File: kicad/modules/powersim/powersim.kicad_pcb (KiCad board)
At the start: 2 copper layers, 84.6 x 64 mm, 61 parts, among them J1 Bus_PCI_Express_x1, J4 Conn_01x02, J6 USB_C_Receptacle_USB2.0_16P, U2 RP2040, U4 W25Q128JVP, U5 BMP388, U8 BNO055, U9 MCP25625T-E/ML, X1 ABM8-272-T3, Y1 ABS07-32.768KHZ-T, Y2 X322516MLB4SI

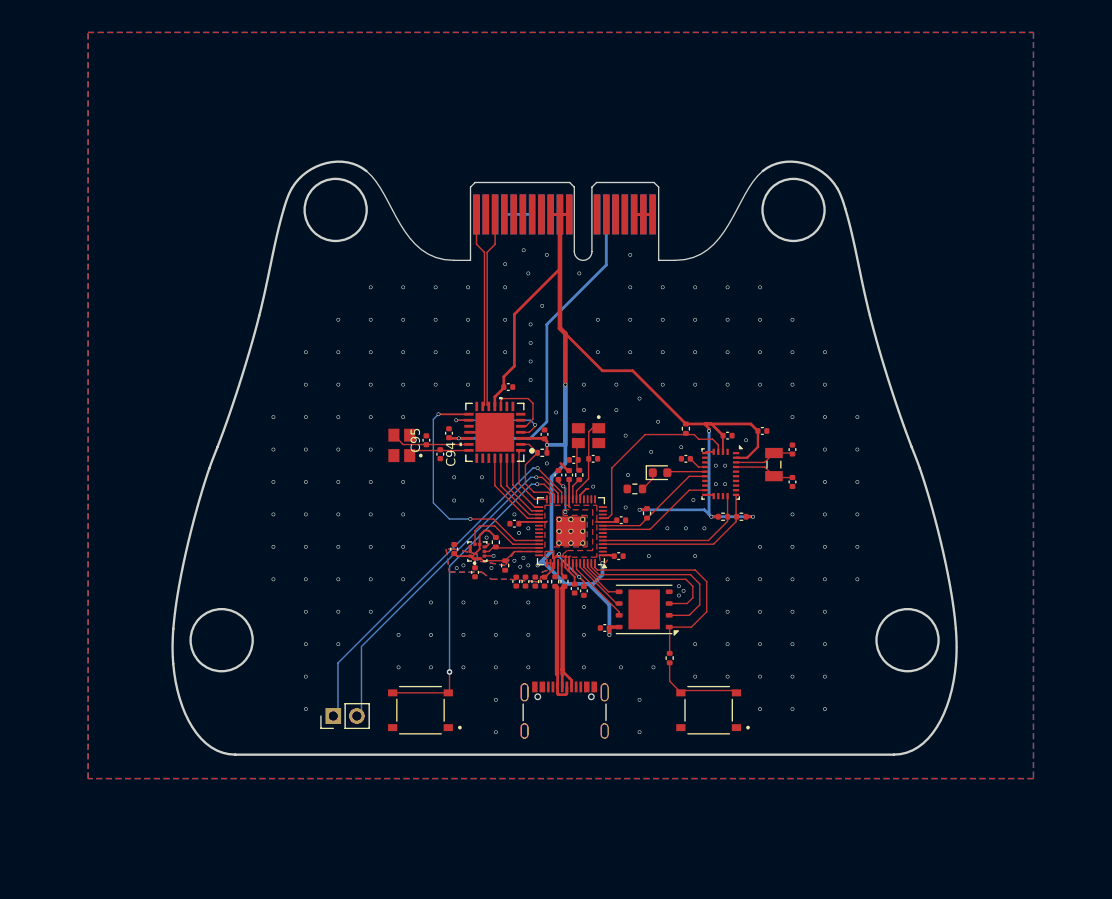
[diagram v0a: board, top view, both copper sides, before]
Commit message: powersim: add all components to schematic
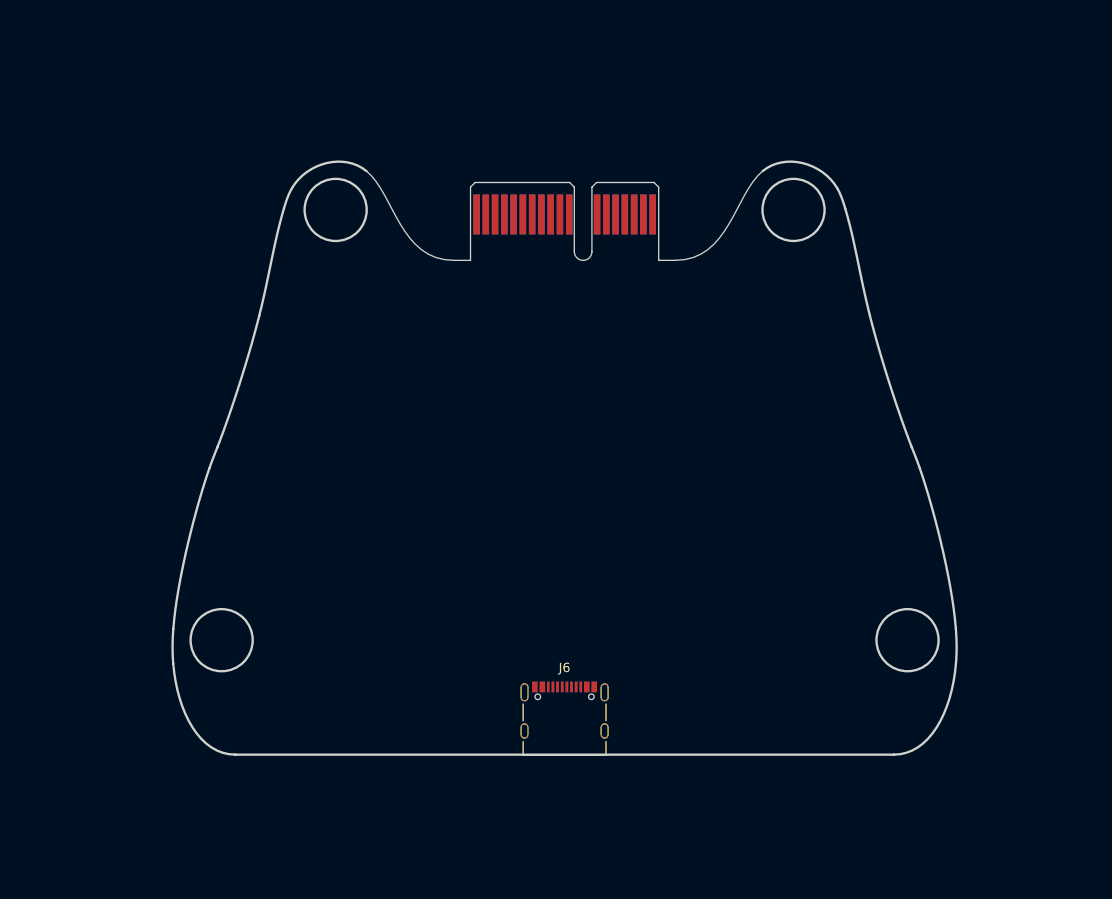
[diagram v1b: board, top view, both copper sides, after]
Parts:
- removed ? (x9): , 
- removed C10, C11: 15p, Capacitor_SMD:C_0402_1005Metric
- removed C206, C207, C209, C211, C212, C213, C214, C215, C216, C40, C50, C51, C81, C82, C90, C92, C93: 100n, Capacitor_SMD:C_0402_1005Metric
- removed C208, C210, C84: 1u, Capacitor_SMD:C_0402_1005Metric
- removed C85, C86, C94, C95: 22p, Capacitor_SMD:C_0402_1005Metric
- removed D88: LED, LED_SMD:LED_0603_1608Metric
- removed J4: Conn_01x02, Connector_PinHeader_2.54mm:PinHeader_1x02_P2.54mm_Vertical
- removed R12, R30: 1k, Resistor_SMD:R_0402_1005Metric
- removed R203, R204: 27, Resistor_SMD:R_0402_1005Metric
- removed R220, R221, R222, R223: 4.7k, Resistor_SMD:R_0402_1005Metric
- removed R83, R87, R91: 10k, Resistor_SMD:R_0402_1005Metric
- removed R89: 150, Resistor_SMD:R_0603_1608Metric
- removed S1, S2: TS-1187A-B-A-B, TS-1187A-B-A-B:SW_TS-1187A-B-A-B
- removed U2: RP2040, Package_DFN_QFN:QFN-56-1EP_7x7mm_P0.4mm_EP3.2x3.2mm
- removed U4: W25Q128JVP, Package_SON:WSON-8-1EP_6x5mm_P1.27mm_EP3.4x4.3mm
- removed U5: BMP388, BMP388:PQFN50P200X200X80-10N
- removed U8: BNO055, Package_LGA:LGA-28_5.2x3.8mm_P0.5mm
- removed U9: MCP25625T-E/ML, MCP25625T_E_ML:QFN28_6X6MC_MCH
- removed X1: ABM8-272-T3, ABM8-272-T3:ABM8-272-T3_ABR
- removed Y1: ABS07-32.768KHZ-T, ABS07-32.768KHZ-T:XTAL_ABS07-32.768KHZ-T
- removed Y2: X322516MLB4SI, X322516MLB4SI:OSC_X322516MLB4SI
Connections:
- J6 pad A4: unconnected-(J6-VBUS-PadA4)_1 -> +5V
- J6 pad A6: USB_D+ -> unconnected-(J6-D+-PadA6)
- J6 pad A7: USB_D- -> unconnected-(J6-D--PadA7)
- J6 pad A9: unconnected-(J6-VBUS-PadA4) -> +5V
- J6 pad B4: unconnected-(J6-VBUS-PadA4)_2 -> +5V
- J6 pad B6: USB_D+ -> unconnected-(J6-D+-PadB6)
- J6 pad B7: USB_D- -> unconnected-(J6-D--PadB7)
- J6 pad B9: unconnected-(J6-VBUS-PadA4)_3 -> +5V
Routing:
- net +3.3V: track 168.2 -> 0.00 mm, vias 16 -> 0
- net /SWCLK: track 40.2 -> 0.00 mm, vias 1 -> 0
- net +5V: track 37.4 -> 0.00 mm, vias 1 -> 0
- net /SWD: track 37.4 -> 0.00 mm, vias 1 -> 0
- net /RUN: track 35.6 -> 0.00 mm, vias 2 -> 0
- net CANSTBY: track 26.2 -> 0.00 mm, vias 2 -> 0
- net /QSPI_SS: track 24.0 -> 0.00 mm
- net CANP: track 21.1 -> 0.00 mm
- net CANN: track 21.1 -> 0.00 mm
- net BOOT_LOAD: track 20.3 -> 0.00 mm
- net /QSPI_SD1: track 18.9 -> 0.00 mm
- net SDA1: track 18.3 -> 0.00 mm
- net SCL1: track 17.0 -> 0.00 mm
- net /QSPI_SD2: track 16.7 -> 0.00 mm
- net +1.1V: track 15.0 -> 0.00 mm, vias 4 -> 0
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- removed copper zone on F.Cu, net +1.1V
- removed copper zone on B.Cu, net +3.3V
- removed copper zone on F.Cu, net +3.3V
- removed copper zone on B.Cu, net GND
- removed copper zone on F.Cu, net GND

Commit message: powersim: finish PCB
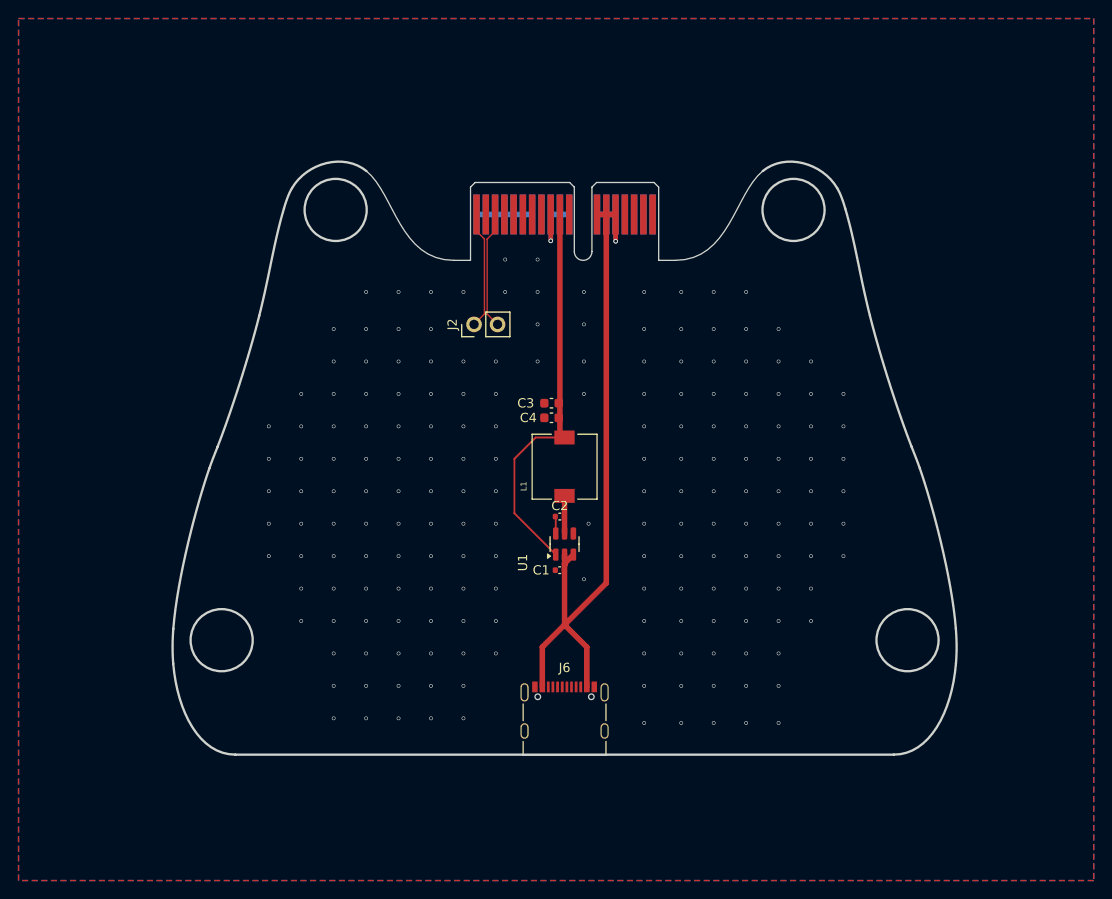
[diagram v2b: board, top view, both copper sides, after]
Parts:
- added C1: 10u, Capacitor_SMD:C_0402_1005Metric, F.Cu at (145.9, 102.5)
- added C2: 100n, Capacitor_SMD:C_0402_1005Metric, F.Cu at (145.9, 96.7)
- added C3: 22u, Capacitor_SMD:C_0603_1608Metric, F.Cu at (145.0, 84.5)
- added C4: 22u, Capacitor_SMD:C_0603_1608Metric, F.Cu at (145.0, 86.1)
- added J2: Conn_01x02_Pin, Connector_PinHeader_2.54mm:PinHeader_1x02_P2.54mm_Vertical, F.Cu at (136.6, 76.0)
- added L1: SLF7055T-6R8N2R8-3PF, SLF7055T-6R8N2R8-3PF:IND_SLF7055T-6R8N2R8-3PF, F.Cu at (146.4, 91.3)
- added U1: AP63203WU, Package_TO_SOT_SMD:TSOT-23-6, F.Cu at (146.4, 99.7)
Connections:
- J1 pad A16: +7.4V -> unconnected-(J1-PERp0-PadA16)
- J1 pad A17: +7.4V -> unconnected-(J1-PERn0-PadA17)
- J1 pad A18: +7.4V -> unconnected-(J1-GND-PadA18)
- J1 pad B16: +7.4V -> unconnected-(J1-GND-PadB16)
- J1 pad B17: +7.4V -> unconnected-(J1-~{PRSNT2}-PadB17)
- J1 pad B18: +7.4V -> unconnected-(J1-GND-PadB18)
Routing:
- net +5V: track 0.00 -> 80.3 mm, vias 0 -> 1
- net +3.3V: track 0.00 -> 50.3 mm, vias 0 -> 1
- net CANN: track 0.00 -> 12.7 mm
- net CANP: track 0.00 -> 12.7 mm
- net GND: track 0.00 -> 6.00 mm, vias 0 -> 187
- net Net-(U1-SW): track 0.00 -> 4.06 mm
- net Net-(U1-BST): track 0.00 -> 1.85 mm
- added copper zone on B.Cu, net GND
- added copper zone on F.Cu, net GND

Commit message: powersim: finish board
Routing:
- net +3.3V: track 50.3 -> 52.3 mm
- net GND: vias 187 -> 194
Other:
- board text added: "powersim 0.1.0"
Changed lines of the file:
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@@
 			(at 2.5 0 0)
 			(layer "F.SilkS")
+			(hide yes)
 			(effects
 				(font
@@
 			(at 0 1.43 0)
 			(layer "F.Fab")
+			(hide yes)
 			(effects
 				(font
@@
 			(at 0 0 0)
 			(layer "F.Fab")
+			(hide yes)
 			(effects
 				(font
@@
 			(at 2.775 0 0)
 			(layer "F.SilkS")
+			(hide yes)
 			(effects
 				(font
@@
 			(at 0 1.43 0)
 			(layer "F.Fab")
+			(hide yes)
 			(effects
 				(font
@@
 			(at 0 0 0)
 			(layer "F.Fab")
+			(hide yes)
 			(effects
 				(font
@@
 			(at 0 -4.58 0)
 			(layer "F.SilkS")
+			(hide yes)
 			(effects
 				(font
@@
 			(at 0 6.24 0)
 			(layer "F.Fab")
+			(hide yes)
 			(effects
 				(font
@@
 		(attr smd)
 		(fp_line
-			(start -4.47 -0.67)
-			(end -4.47 1.13)
-			(stroke
-				(width 0.12)
-				(type solid)
-			)
-			(layer "F.SilkS")
-		)
-		(fp_line
-			(start -4.47 4.84)
-			(end -4.47 3.38)
-			(stroke
-				(width 0.12)
-				(type solid)
-			)
-			(layer "F.SilkS")
-		)
-		(fp_line
-			(start 4.47 -0.67)
-			(end 4.47 1.13)
-			(stroke
-				(width 0.12)
-				(type solid)
-			)
-			(layer "F.SilkS")
-		)
-		(fp_line
-			(start 4.47 4.84)
-			(end -4.47 4.84)
-			(stroke
-				(width 0.12)
-				(type solid)
-			)
-			(layer "F.SilkS")
-		)
-		(fp_line
-			(start 4.47 4.84)
-			(end 4.47 3.38)
-			(stroke
-				(width 0.12)
-				(type solid)
-			)
-			(layer "F.SilkS")
-		)
-		(fp_line
 			(start -4.47 4.34)
 			(end 4.47 4.34)
@@
 			(at 0 3.43 0)
 			(layer "Dwgs.User")
+			(hide yes)
 			(effects
 				(font
@@
 			(at 0 1.18 0)
 			(layer "F.Fab")
+			(hide yes)
 			(effects
 				(font
@@
 			(at 0 -1.16 0)
 			(layer "F.SilkS")
+			(hide yes)
 			(effects
 				(font
@@
 			(at 0 1.16 0)
 			(layer "F.Fab")
+			(hide yes)
 			(effects
 				(font
@@
 			(at 0 0 0)
 			(layer "F.Fab")
+			(hide yes)
 			(effects
 				(font
@@
 			(at -2 -4.5 90)
 			(layer "F.SilkS")
+			(hide yes)
 			(effects
 				(font
@@
 			(at 0 2.4 90)
 			(layer "F.Fab")
+			(hide yes)
 			(effects
 				(font
@@
 			(at 0 0 90)
 			(layer "F.Fab")
+			(hide yes)
 			(effects
 				(font
@@
 			(at 0 -2.33 90)
 			(layer "F.SilkS")
+			(hide yes)
 			(effects
 				(font
@@
 			(at 0 4.87 90)
 			(layer "F.Fab")
+			(hide yes)
 			(effects
 				(font
@@
 			(at 0 1.27 0)
 			(layer "F.Fab")
+			(hide yes)
 			(effects
 				(font
@@
 			(at -2.118 -4.4064 90)
 			(layer "F.SilkS")
+			(hide yes)
 			(effects
 				(font
@@
 			(at 5.6036 4.4064 90)
 			(layer "F.Fab")
+			(hide yes)
 			(effects
 				(font
@@
 		(tags "capacitor")
 		(property "Reference" "C1"
-			(at 2 0 360)
+			(at 2 0 0)
 			(layer "F.SilkS")
+			(hide yes)
 			(effects
 				(font
@@
 		)
 		(property "Value" "10u"
-			(at 0 1.16 360)
+			(at 0 1.16 0)
 			(layer "F.Fab")
+			(hide yes)
 			(effects
 				(font
@@
 		)
 		(fp_text user "${REFERENCE}"
-			(at 0 0 360)
+			(at 0 0 0)
 			(layer "F.Fab")
+			(hide yes)
 			(effects
 				(font
@@
 		(layer "Edge.Cuts")
 	)
+	(gr_text "powersim 0.1.0"
+		(at 155 110.5 0)
+		(layer "F.SilkS")
+		(effects
+			(font
+				(size 1 1)
+				(thickness 0.1)
+			)
+			(justify left bottom)
+		)
+	)
 	(segment
 		(start 145.46 98.5625)
@@
 	)
 	(via
+		(at 149 101)
+		(size 0.4)
+		(drill 0.3)
+		(layers "F.Cu" "B.Cu")
+		(free yes)
+		(net 8)
+	)
+	(via
 		(at 173 90.5)
 		(size 0.4)
@@
 	)
 	(via
+		(at 142.5 90.5)
+		(size 0.4)
+		(drill 0.3)
+		(layers "F.Cu" "B.Cu")
+		(free yes)
+		(net 8)
+	)
+	(via
 		(at 159 80)
 		(size 0.4)
@@
 	)
 	(via
+		(at 149 87)
+		(size 0.4)
+		(drill 0.3)
+		(layers "F.Cu" "B.Cu")
+		(free yes)
+		(net 8)
+	)
+	(via
 		(at 162.5 97.5)
 		(size 0.4)
@@
 	)
 	(via
+		(at 142.5 94)
+		(size 0.4)
+		(drill 0.3)
+		(layers "F.Cu" "B.Cu")
+		(free yes)
+		(net 8)
+	)
+	(via
 		(at 162.5 115)
 		(size 0.4)
@@
 	)
 	(via
-		(at 148.5 103.5)
+		(at 148 104.5)
 		(size 0.4)
 		(drill 0.3)
@@
 	)
 	(via
+		(at 149 90.5)
+		(size 0.4)
+		(drill 0.3)
+		(layers "F.Cu" "B.Cu")
+		(free yes)
+		(net 8)
+	)
+	(via
 		(at 162.5 83.5)
 		(size 0.4)
@@
 	)
 	(via
+		(at 149 94)
+		(size 0.4)
+		(drill 0.3)
+		(layers "F.Cu" "B.Cu")
+		(free yes)
+		(net 8)
+	)
+	(via
 		(at 155 101)
 		(size 0.4)
@@
 	)
 	(via
+		(at 143.5 97)
+		(size 0.4)
+		(drill 0.3)
+		(layers "F.Cu" "B.Cu")
+		(free yes)
+		(net 8)
+	)
+	(via
 		(at 155 83.5)
 		(size 0.4)
@@
 		(layer "F.Cu")
 		(net 9)
+	)
+	(segment
+		(start 144.913 64.138595)
+		(end 146.913 64.138595)
+		(width 0.5)
+		(layer "F.Cu")
+		(net 9)

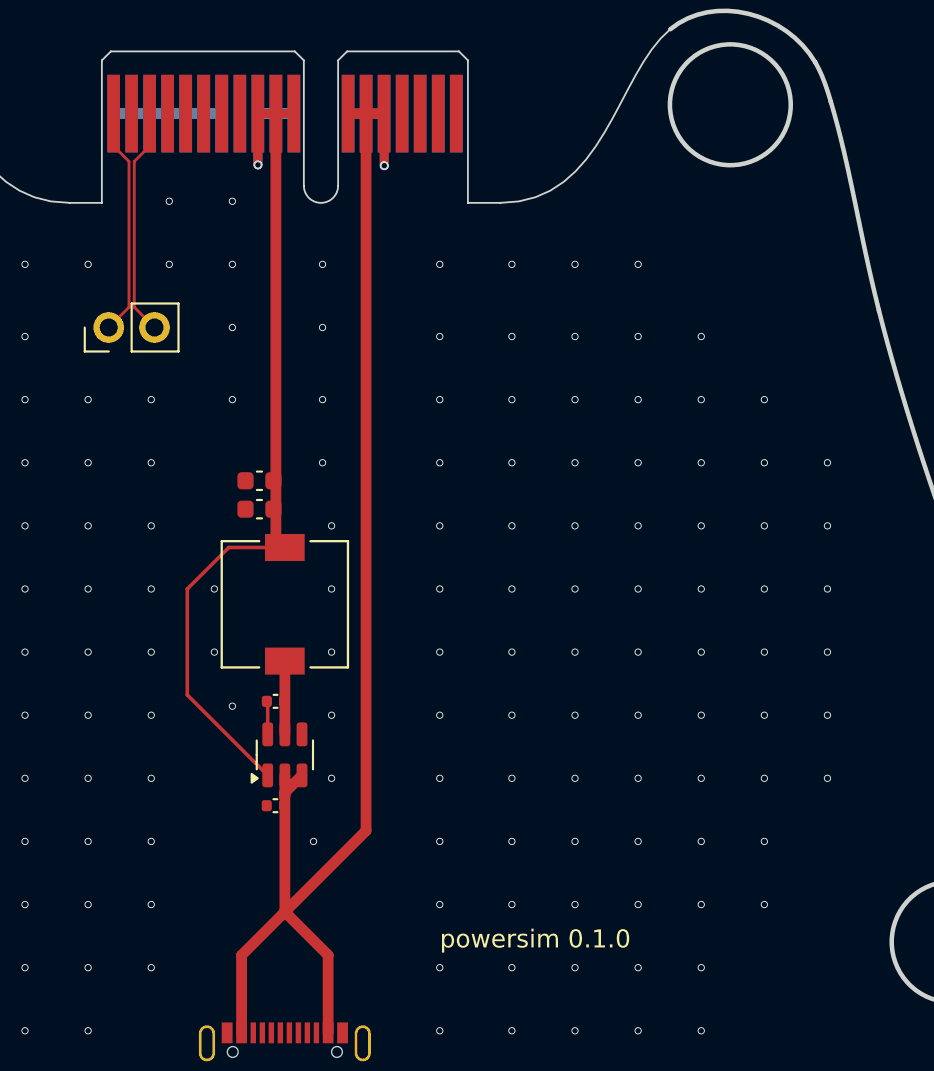
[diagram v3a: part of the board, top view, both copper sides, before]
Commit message: powersim: generate final production files
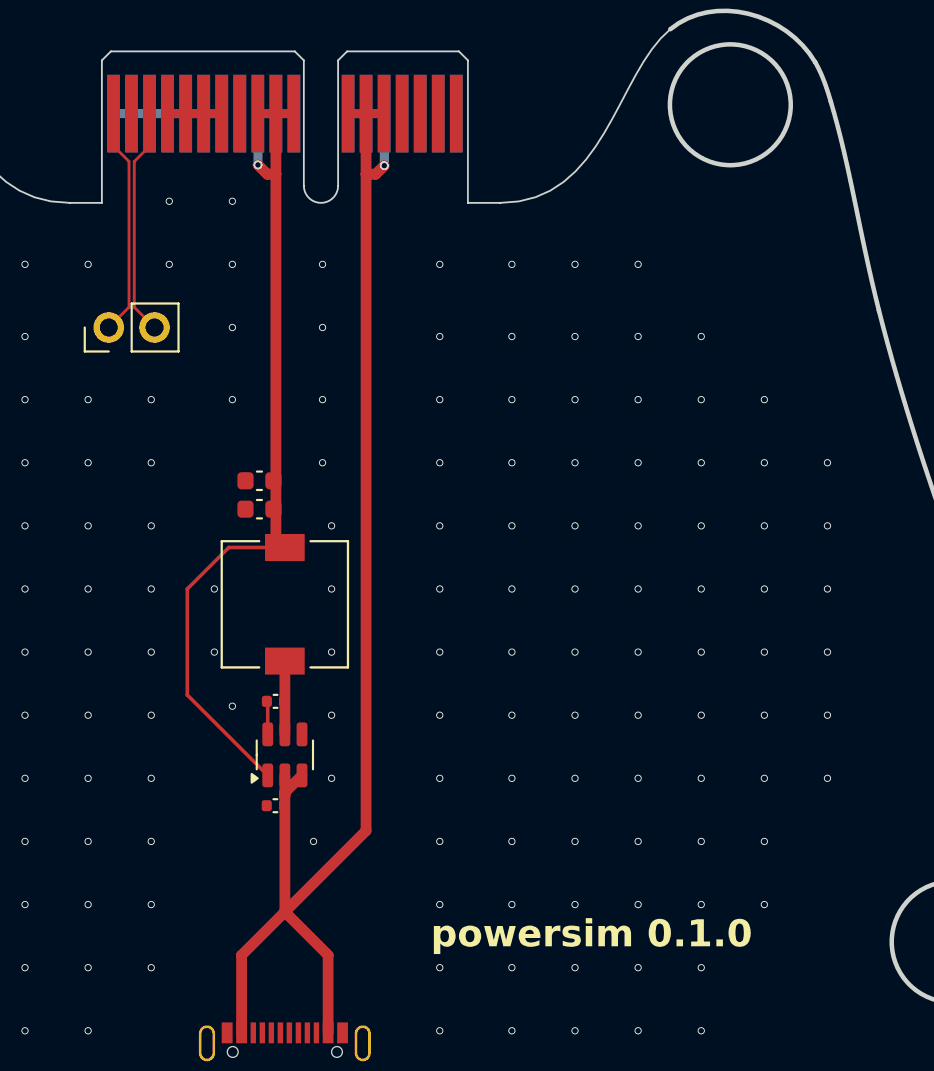
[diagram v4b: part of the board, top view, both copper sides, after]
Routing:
- net GND: track 6.00 -> 9.00 mm
- net +5V: track 80.3 -> 78.6 mm
- net +3.3V: track 52.3 -> 50.7 mm
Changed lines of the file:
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@@
 	)
 	(gr_text "powersim 0.1.0"
-		(at 155 110.5 0)
+		(at 154.5 110.5 0)
 		(layer "F.SilkS")
 		(effects
 			(font
-				(size 1 1)
-				(thickness 0.1)
+				(size 1.5 1.5)
+				(thickness 0.3)
+				(bold yes)
 			)
 			(justify left bottom)
@@
 		(net 2)
 	)
+	(segment
+		(start 142.913 64.138595)
+		(end 139.913 64.138595)
+		(width 0.5)
+		(layer "F.Cu")
+		(net 8)
+	)
 	(via
 		(at 166 97.5)
@@
 		(start 142.913 64.138595)
 		(end 136.913 64.138595)
+		(width 0.5)
+		(layer "B.Cu")
+		(net 8)
+	)
+	(segment
+		(start 145.913 87.703)
+		(end 145.913 67.5)
 		(width 0.6)
-		(layer "B.Cu")
-		(net 8)
+		(layer "F.Cu")
+		(net 9)
 	)
 	(segment
@@
 	)
 	(segment
-		(start 145.913 87.703)
-		(end 145.913 64.25)
-		(width 0.6)
-		(layer "F.Cu")
-		(net 9)
-	)
-	(segment
 		(start 145.46 100.8375)
 		(end 141 96.3775)
@@
 	)
 	(segment
+		(start 145.913 67.5)
+		(end 145.435529 67.5)
+		(width 0.6)
+		(layer "F.Cu")
+		(net 9)
+	)
+	(segment
+		(start 145.913 67.5)
+		(end 145.913 64.25)
+		(width 0.6)
+		(layer "F.Cu")
+		(net 9)
+	)
+	(segment
 		(start 141 90.5)
 		(end 143.3 88.2)
@@
 	)
 	(segment
-		(start 144.918787 66.983258)
-		(end 144.918787 64.144382)
-		(width 0.5)
+		(start 145.435529 67.5)
+		(end 144.918787 66.983258)
+		(width 0.6)
 		(layer "F.Cu")
 		(net 9)
@@
 		(start 144.913 64.138595)
 		(end 146.863 64.138595)
-		(width 0.6)
+		(width 0.5)
 		(layer "B.Cu")
 		(net 9)
@@
 	)
 	(segment
-		(start 151.923458 67.025633)
-		(end 151.923458 64.149053)
-		(width 0.5)
-		(layer "F.Cu")
-		(net 10)
-	)
-	(segment
 		(start 150.913 64.138595)
 		(end 151.913 64.138595)
-		(width 0.6)
+		(width 0.5)
 		(layer "F.Cu")
 		(net 10)
@@
 	)
 	(segment
+		(start 151.449091 67.5)
+		(end 151.923458 67.025633)
+		(width 0.6)
+		(layer "F.Cu")
+		(net 10)
+	)
+	(segment
 		(start 150.913 64.138595)
 		(end 149.963 64.138595)
-		(width 0.6)
+		(width 0.5)
 		(layer "F.Cu")
 		(net 10)
@@
 	(segment
 		(start 150.913 103.907)
+		(end 150.913 67.5)
+		(width 0.6)
+		(layer "F.Cu")
+		(net 10)
+	)
+	(segment
+		(start 150.913 67.5)
+		(end 151.449091 67.5)
+		(width 0.6)
+		(layer "F.Cu")
+		(net 10)
+	)
+	(segment
+		(start 150.913 67.5)
 		(end 150.913 64.138595)
 		(width 0.6)
@@
 		(start 151.913 64.138595)
 		(end 149.963 64.138595)
-		(width 0.6)
+		(width 0.5)
 		(layer "B.Cu")
 		(net 10)
